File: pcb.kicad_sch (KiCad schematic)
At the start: 23 parts, among them SW1 SW_Push, SW2 SW_Push, U1 Pico

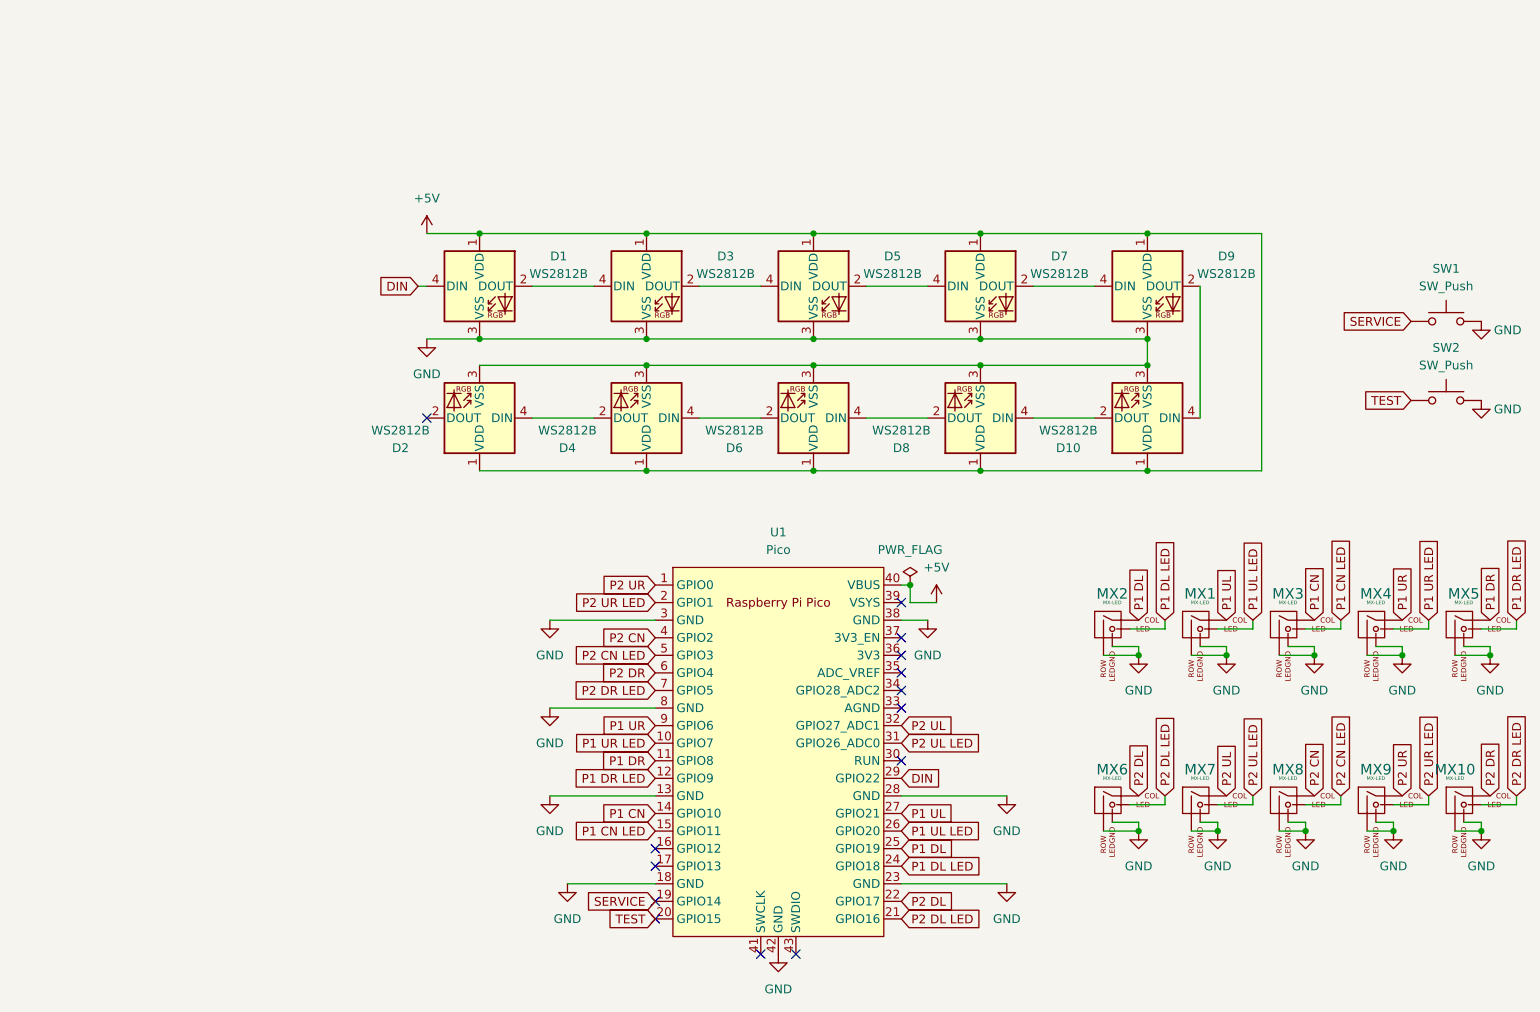
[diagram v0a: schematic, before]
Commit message: Clean up trace routing
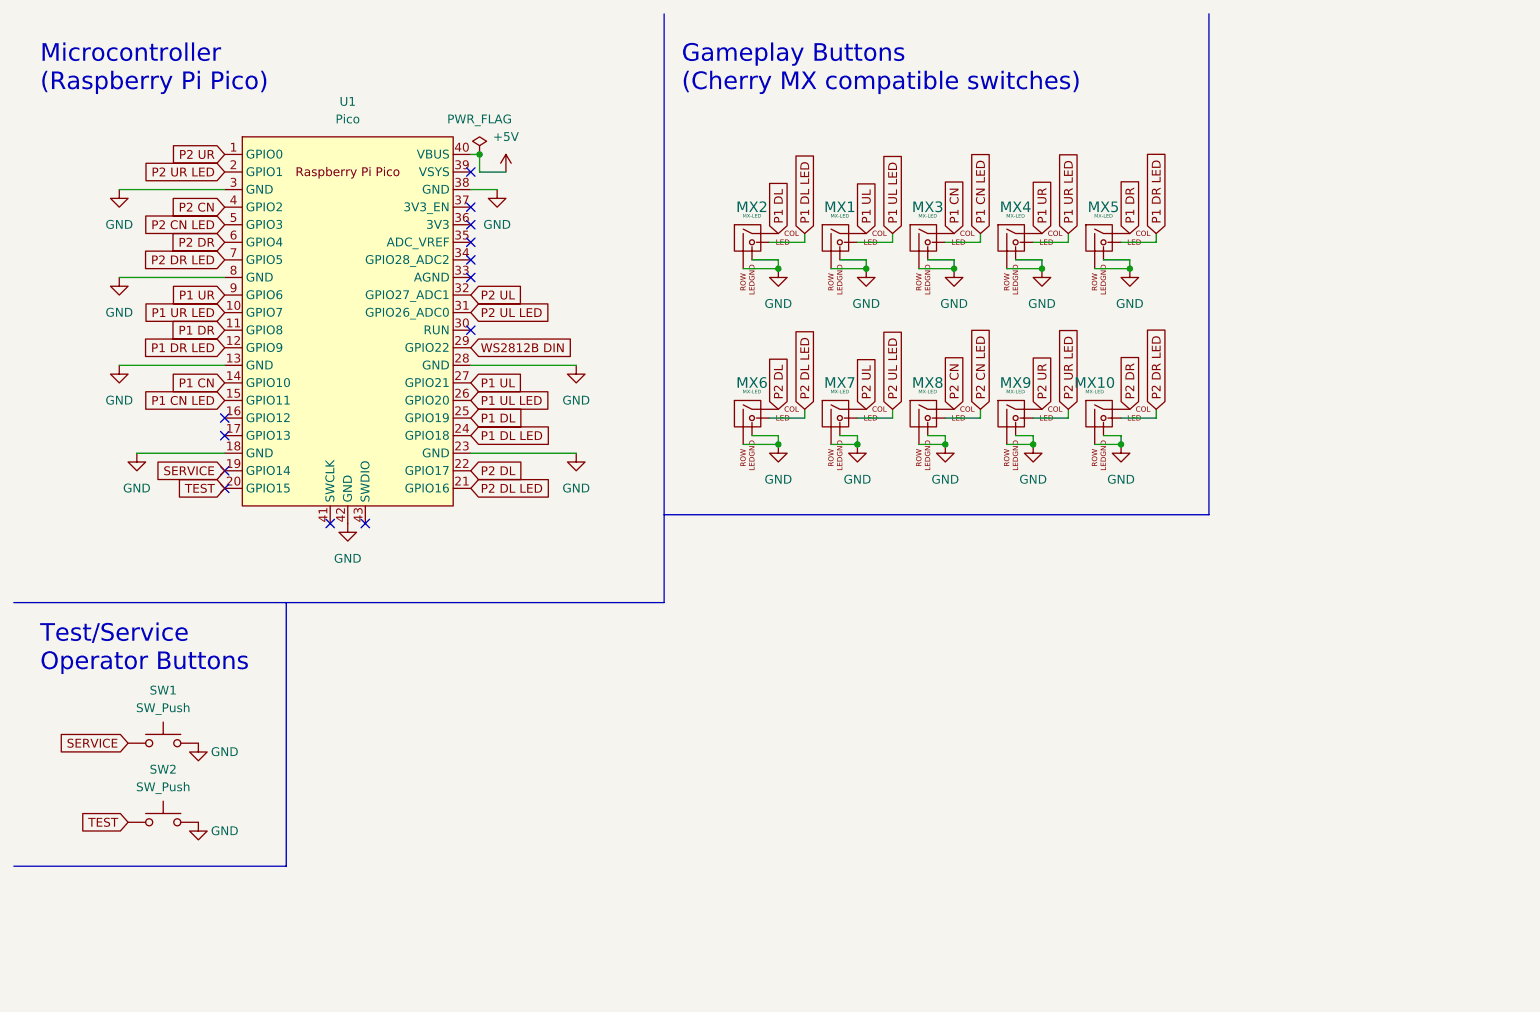
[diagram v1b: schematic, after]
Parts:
- removed D1, D10, D2, D3, D4, D5, D6, D7, D8, D9: WS2812B, LED_SMD:LED_WS2812B_PLCC4_5.0x5.0mm_P3.2mm, symbol LED:WS2812B
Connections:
- net DIN renamed WS2812B DIN
- no-connect marks 14 -> 13
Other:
- note added: "Gameplay Buttons (Cherry MX compatible switches)"
- note added: "Microcontroller (Raspberry Pi Pico)"
- note added: "Test/Service Operator Buttons"
- moved on the sheet: MX1, MX10, MX2, MX3, MX4, MX5, MX6, MX7, MX8, MX9, SW1, SW2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

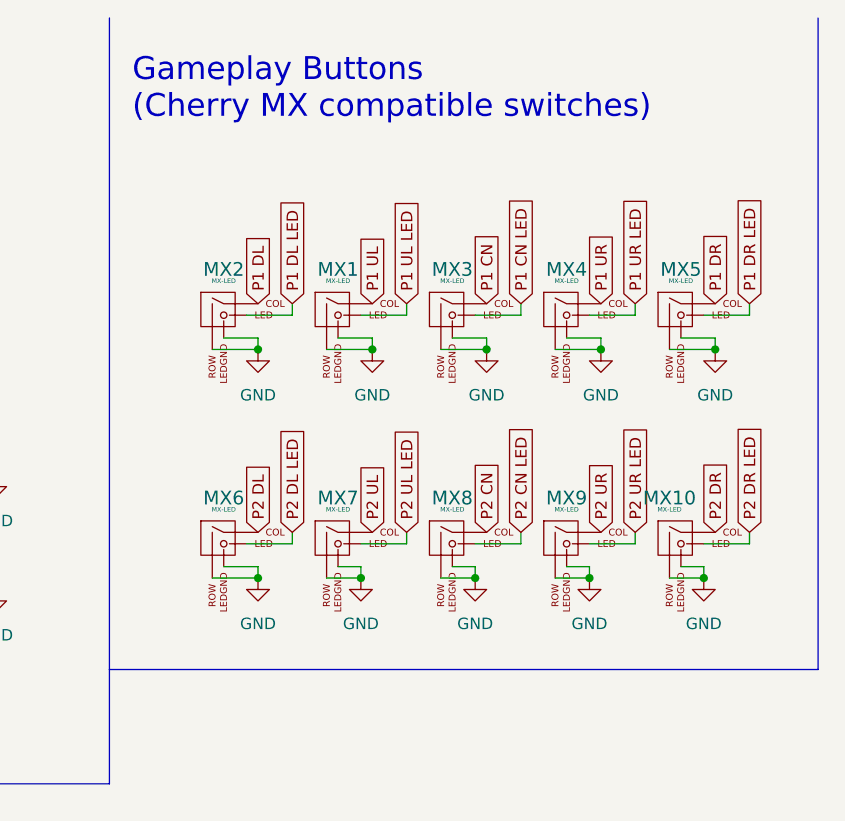
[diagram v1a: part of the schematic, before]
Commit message: Add resistors to LEDs, general cleanup/updates
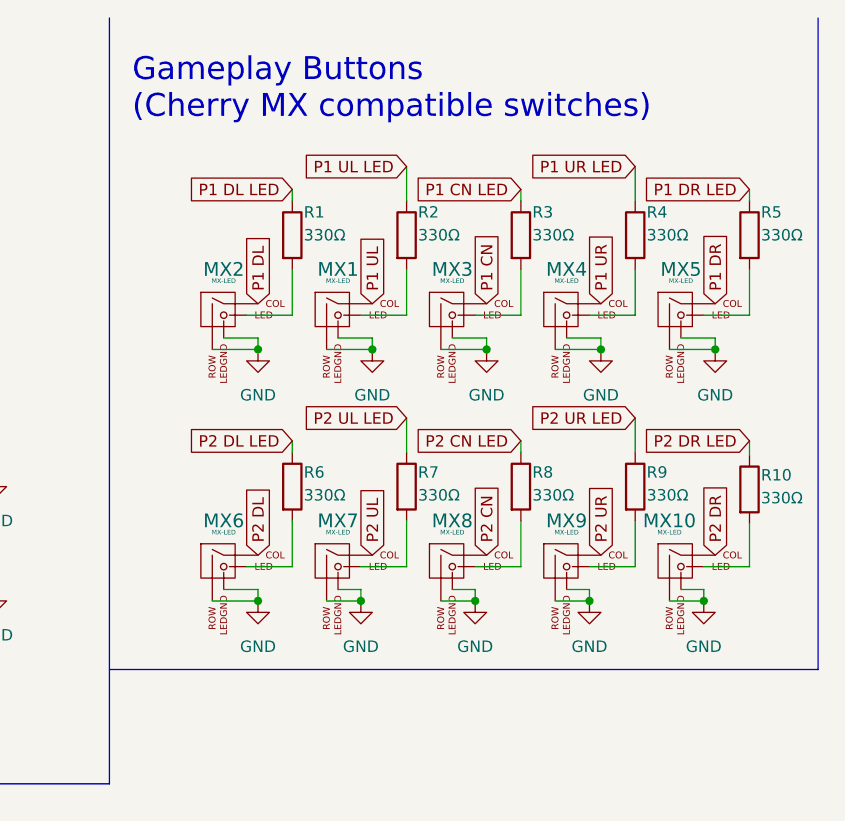
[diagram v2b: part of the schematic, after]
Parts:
- added R1, R10, R2, R3, R4, R5, R6, R7, R8, R9: 330Ω, Resistor_SMD:R_0805_2012Metric_Pad1.20x1.40mm_HandSolder, symbol Device:R
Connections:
- net P1 CN LED: now also R3.1; no longer MX3.3 (LED)
- net P1 DL LED: now also R1.1; no longer MX2.3 (LED)
- net P1 DR LED: now also R5.1; no longer MX5.3 (LED)
- net P1 UL LED: now also R2.1; no longer MX1.3 (LED)
- net P1 UR LED: now also R4.1; no longer MX4.3 (LED)
- net P2 CN LED: now also R8.1; no longer MX8.3 (LED)
- net P2 DL LED: now also R6.1; no longer MX6.3 (LED)
- net P2 DR LED: now also R10.1; no longer MX10.3 (LED)
- net P2 UL LED: now also R7.1; no longer MX7.3 (LED)
- net P2 UR LED: now also R9.1; no longer MX9.3 (LED)
- new net: MX3.3 (LED), R3.2
- new net: MX5.3 (LED), R5.2
- new net: MX6.3 (LED), R6.2
- new net: MX7.3 (LED), R7.2
- new net: MX10.3 (LED), R10.2
- new net: MX9.3 (LED), R9.2
- new net: MX4.3 (LED), R4.2
- new net: MX1.3 (LED), R2.2
- new net: MX2.3 (LED), R1.2
- new net: MX8.3 (LED), R8.2
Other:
- moved on the sheet: MX10, MX6, MX7, MX8, MX9
